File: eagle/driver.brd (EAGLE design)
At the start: 101.6 x 76.2 mm, 96 parts, among them IC1 XMEGA128A1, IC10 ST95P08M, IC11 ST95P08M, IC12 ST95P08M, IC13 ST95P08M, IC14 ST95P08M, IC15 ST95P08M, IC16 74AHC1G02DBV, IC17 74AHC1G02DBV, IC18 74AHC1G125DBV, IC19 74AHC1G125DBV, IC2 74AC16244, IC20 ST95P08M, IC21 ST95P08M, IC22 ST95P08M, IC23 ST95P08M, IC24 ST95P08M, IC25 ST95P08M, IC3 74AC16244, IC4 74AC16244, IC5 74AC16244, IC6 74AC16374, IC7 74AC16374, IC8 74AC16374, IC9 74AC16374, SW1 FSM2JSMA

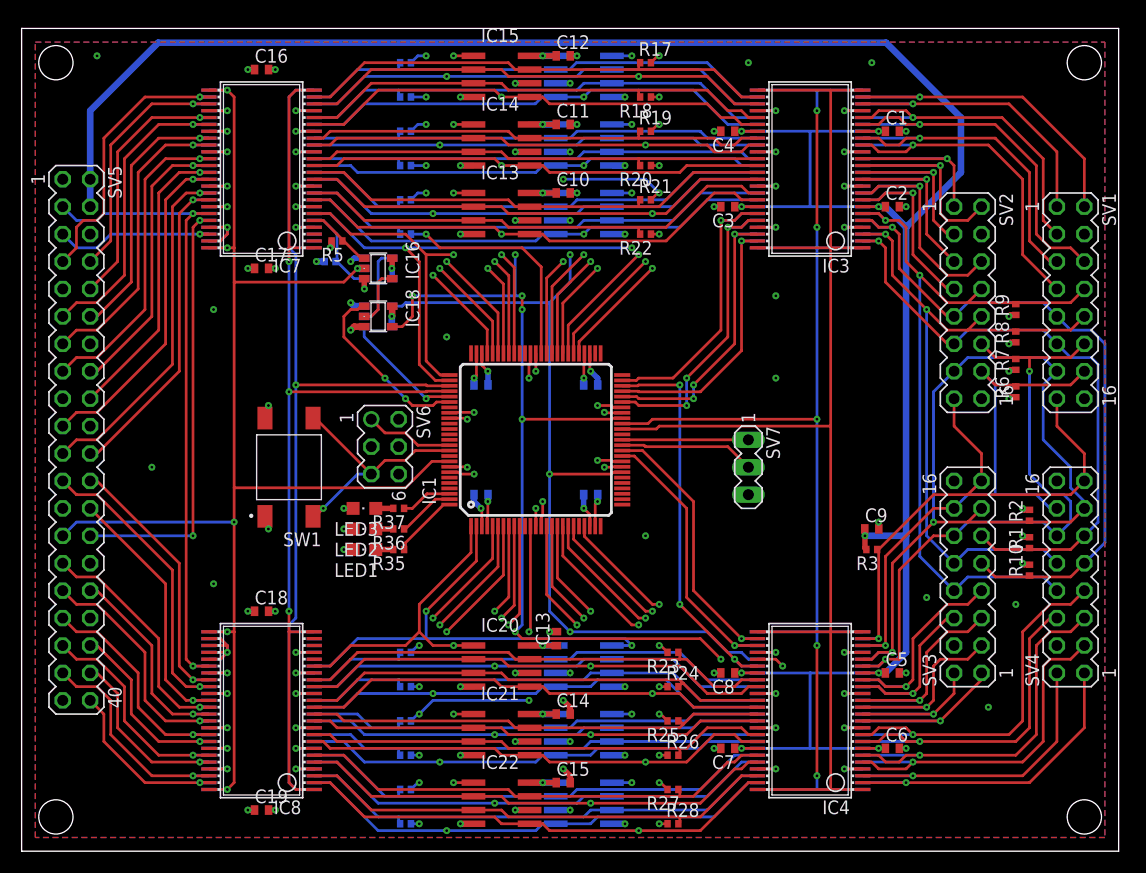
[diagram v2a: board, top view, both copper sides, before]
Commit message: adjust spacing of 16-pin headers
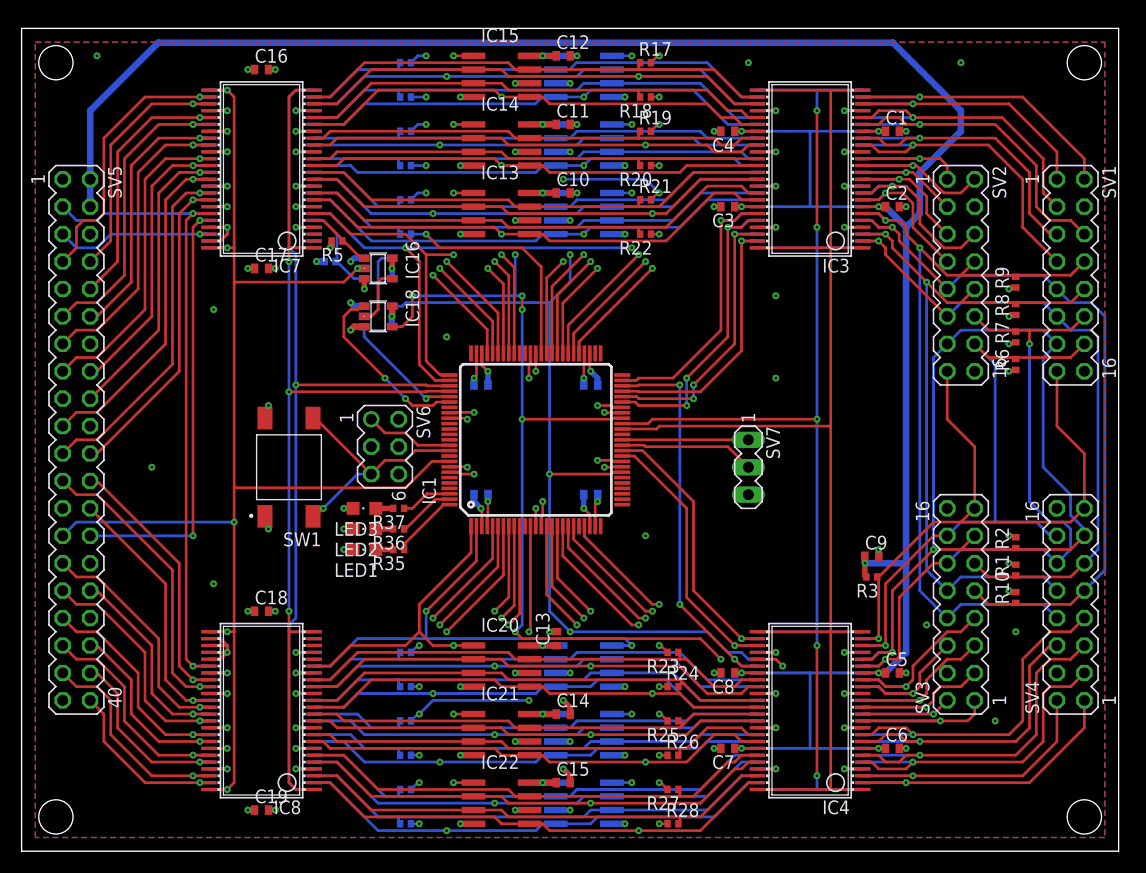
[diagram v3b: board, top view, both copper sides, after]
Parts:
- moved R1 2.84 mm to (92.1, 26.0)
- moved R10 2.84 mm to (92.1, 23.5)
- moved R2 2.84 mm to (92.1, 28.6)
- moved SV2 2.62 mm to (87.0, 53.3)
- moved SV3 2.62 mm to (87.0, 22.9)
- moved SV1 2.54 mm to (97.2, 53.3)
- moved R3 2.54 mm to (78.7, 25.4)
- moved C9 2.54 mm to (78.7, 27.3)
- moved R6 2.54 mm to (92.1, 45.1)
- moved R7 2.54 mm to (92.1, 47.6)
- moved R8 2.54 mm to (92.1, 50.2)
- moved R9 2.54 mm to (92.1, 52.7)
- moved SV4 2.54 mm to (97.2, 22.9)
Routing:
- net N$20: track 76.2 -> 84.2 mm
- net N$21: track 52.2 -> 59.8 mm
- net N$7: track 23.4 -> 16.6 mm
- net N$9: track 20.0 -> 13.2 mm
- net N$10: track 24.1 -> 17.8 mm
- net N$18: track 20.7 -> 14.4 mm
- net N$8: track 20.5 -> 14.2 mm
- net N$13: track 20.4 -> 14.6 mm
- net N$27: track 53.9 -> 57.3 mm
- net N$14: track 58.0 -> 61.2 mm
- net N$38: track 18.8 -> 15.6 mm
- net N$39: track 21.5 -> 18.3 mm
- net N$36: track 21.1 -> 18.0 mm
- net N$17: track 61.3 -> 64.5 mm
- net N$37: track 21.7 -> 18.5 mm
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
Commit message: add pull ups for register and buffer output enable lines
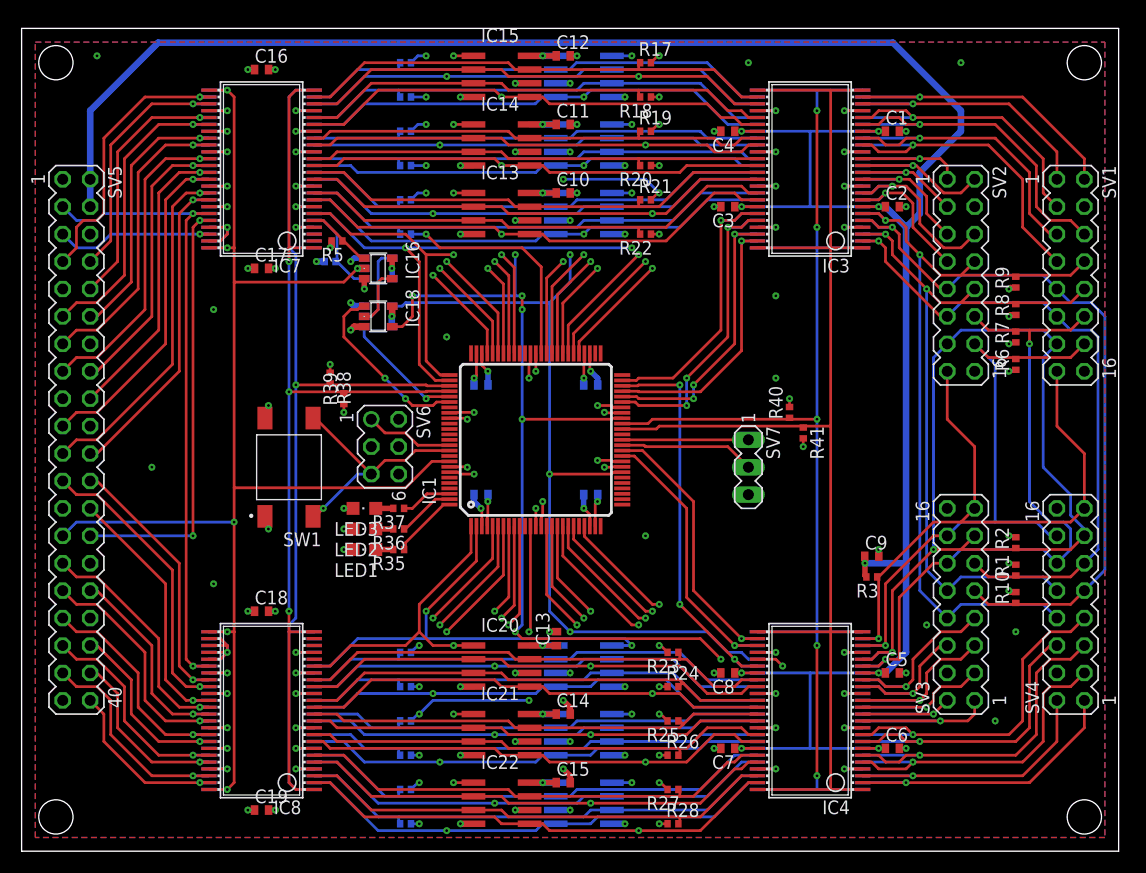
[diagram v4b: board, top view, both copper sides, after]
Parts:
- added R38, R39, R40, R41: 33k, rcl:R0402
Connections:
- net N$16: now also R41.1
- net N$19: now also R40.1
- net N$48: now also R38.2
- net N$56: now also R39.2
- net VCC: now also R38.1, R39.1, R40.2, R41.2
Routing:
- net VCC: track 83.0 -> 86.1 mm, vias 32 -> 36

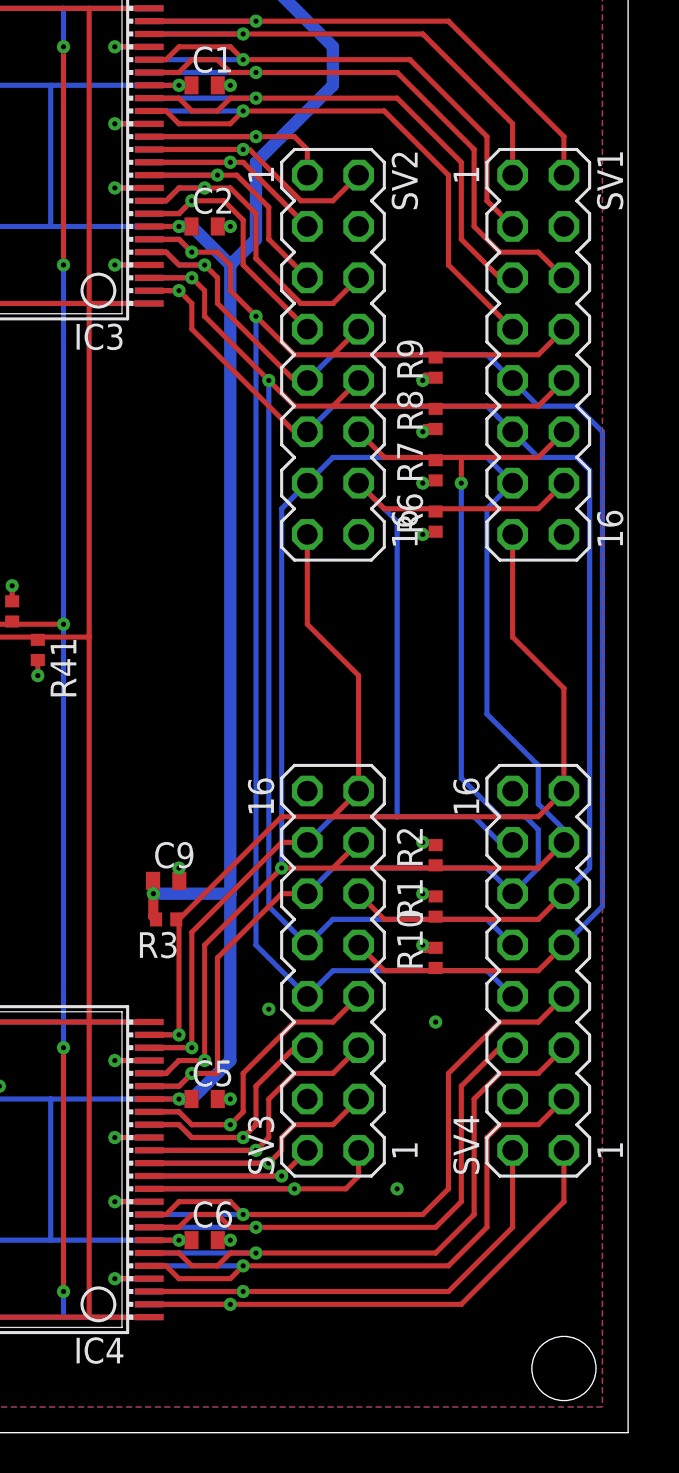
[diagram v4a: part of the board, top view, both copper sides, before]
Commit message: more spacing between panel headers
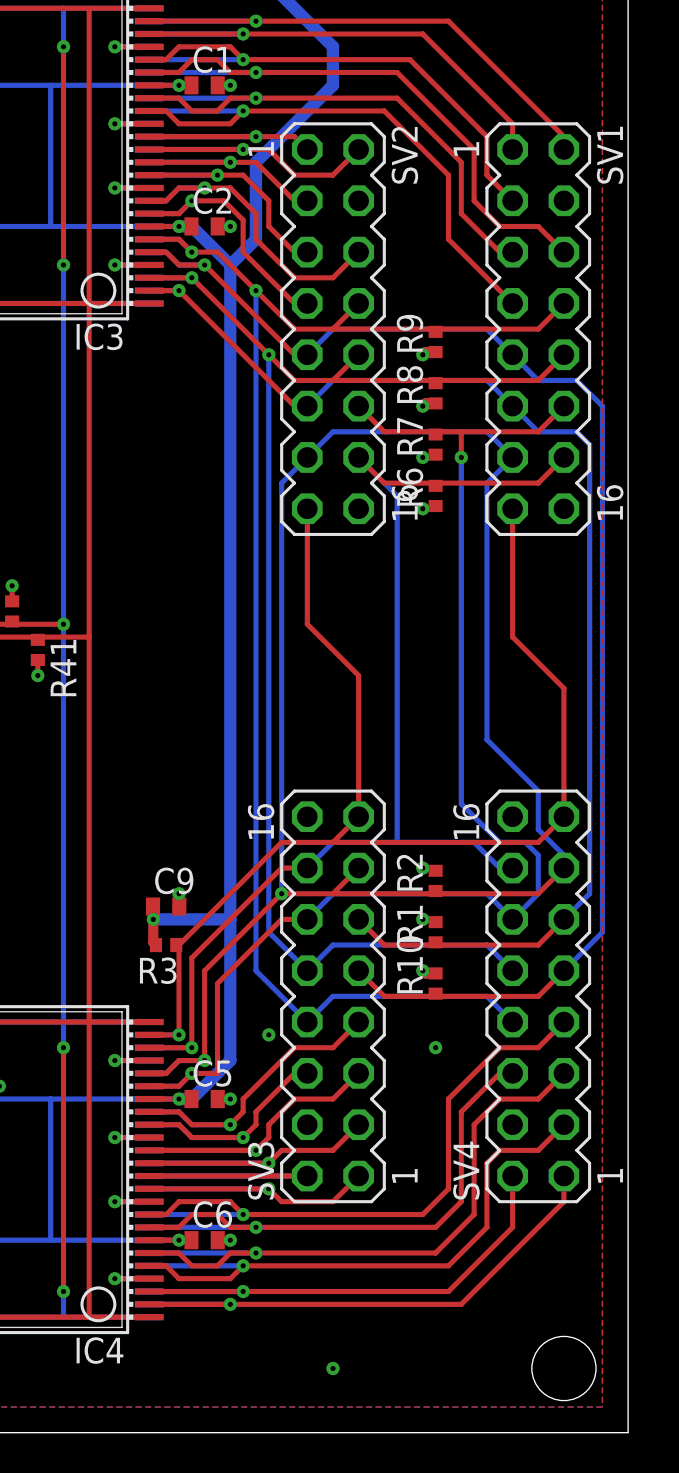
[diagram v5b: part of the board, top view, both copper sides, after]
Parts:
- moved R7 1.27 mm to (92.1, 48.9)
- moved R8 1.27 mm to (92.1, 51.4)
- moved R9 1.27 mm to (92.1, 54.0)
- moved C9 1.27 mm to (78.7, 26.0)
- moved R1 1.27 mm to (92.1, 24.8)
- moved R10 1.27 mm to (92.1, 22.2)
- moved R2 1.27 mm to (92.1, 27.3)
- moved R3 1.27 mm to (78.7, 24.1)
- moved SV3 1.27 mm to (87.0, 21.6)
- moved SV4 1.27 mm to (97.2, 21.6)
- moved R6 1.27 mm to (92.1, 46.4)
- moved SV1 1.27 mm to (97.2, 54.6)
- moved SV2 1.27 mm to (87.0, 54.6)
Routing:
- net N$20: track 84.2 -> 88.0 mm
- net N$21: track 59.8 -> 63.6 mm
- net N$32: track 19.1 -> 17.1 mm
- net N$11: track 74.4 -> 75.7 mm
- net N$17: track 64.5 -> 65.8 mm
- net N$6: track 30.2 -> 29.0 mm
- net N$5: track 29.7 -> 28.4 mm
- net N$28: track 33.5 -> 32.2 mm
- net N$25: track 33.9 -> 32.6 mm
- net N$23: track 29.2 -> 27.9 mm
- net N$2: track 27.0 -> 25.7 mm
- net N$14: track 61.6 -> 62.8 mm
- net N$13: track 14.6 -> 13.4 mm
- net N$1: track 30.1 -> 28.8 mm
- net N$4: track 28.4 -> 27.2 mm
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
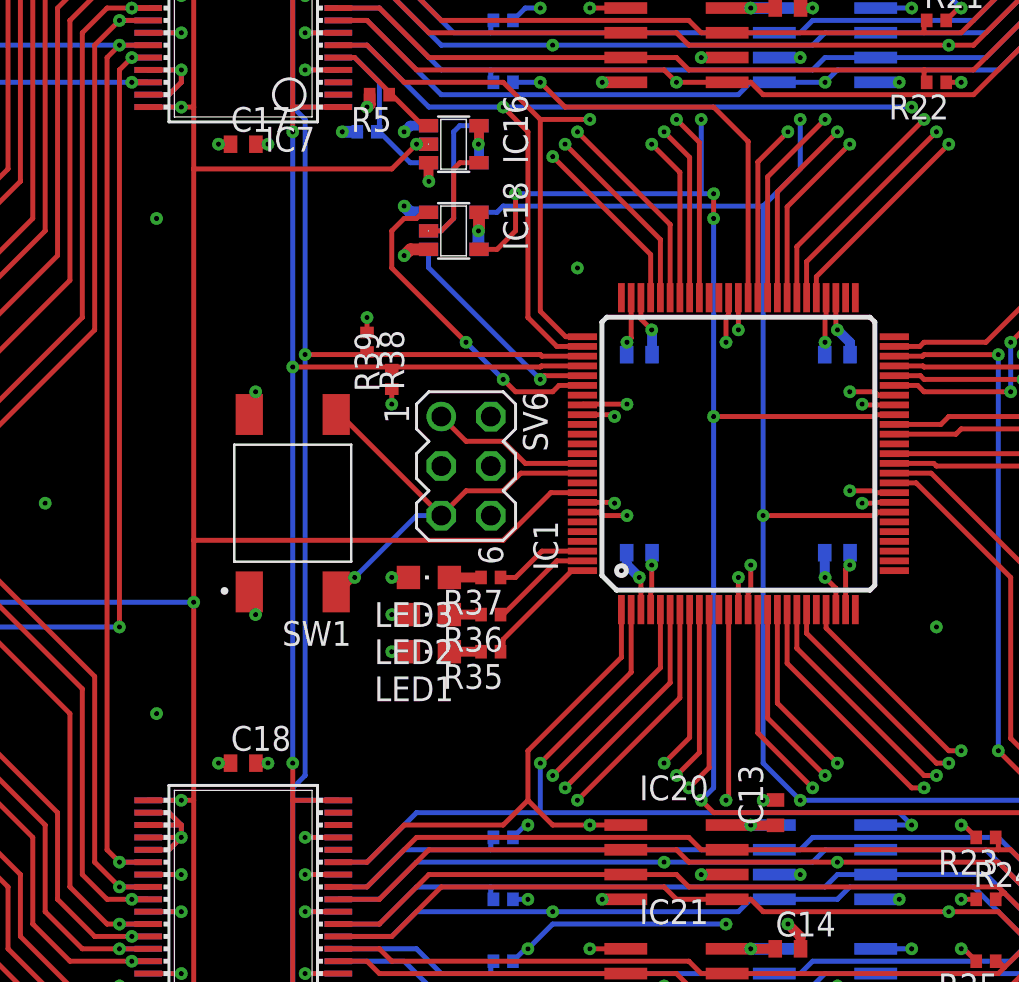
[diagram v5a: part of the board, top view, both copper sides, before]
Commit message: consolidate duplicate signals on board
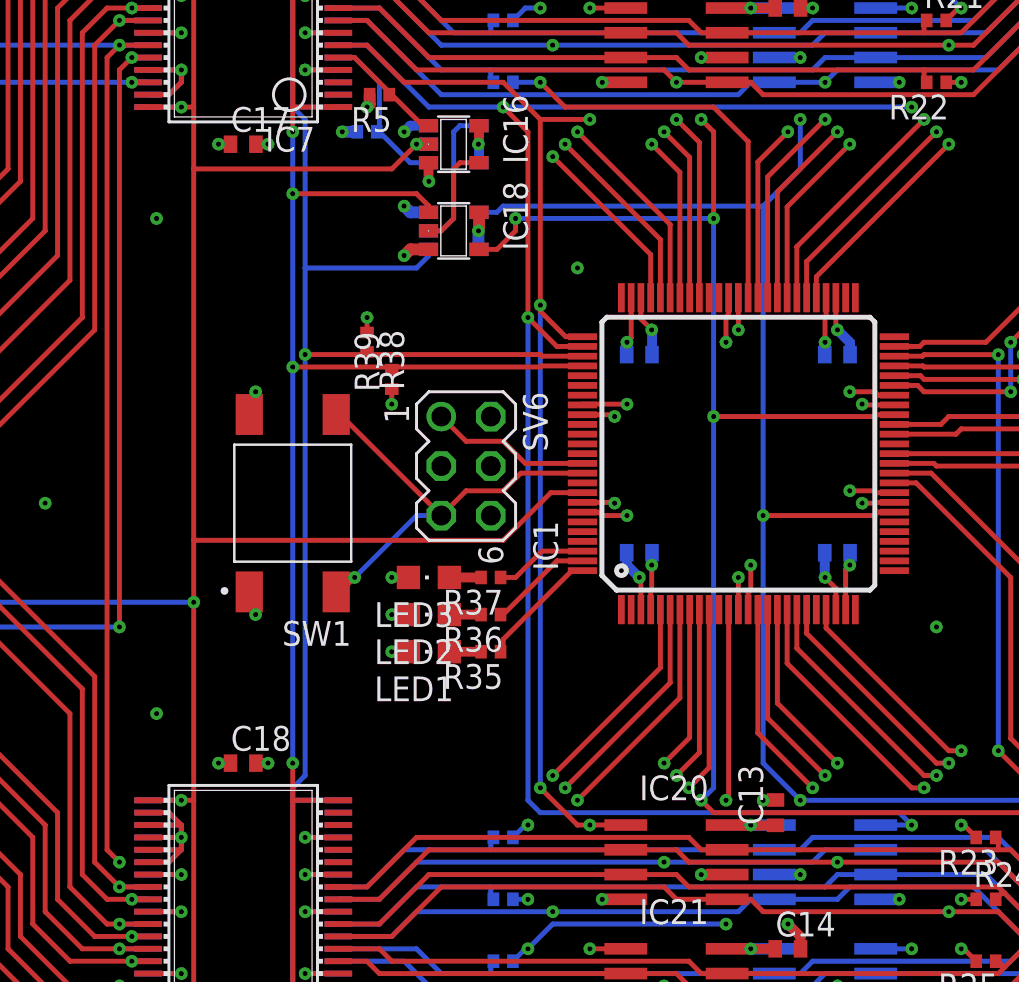
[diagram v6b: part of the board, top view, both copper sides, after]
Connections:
- net N$16 renamed OEN1
- net N$19 renamed OEN0
- removed net CLK_EN0: IC1.80, IC19.1
- removed net CLK_EN1: IC1.81, IC18.1
- removed net N$48: IC1.78, IC6.1, IC6.24, IC9.1, IC9.24, R38.2
- removed net N$56: IC1.79, IC7.1, IC7.24, IC8.1, IC8.24, R39.2
- removed net VSYNC2: IC1.1, IC20.1, IC21.1, IC22.1, IC8.19
- removed net VSYNC3: IC1.2, IC23.1, IC24.1, IC25.1, IC9.6
- new net IEN0: IC1.78, IC19.1, IC6.1, IC6.24, IC9.1, IC9.24, R38.2
- new net IEN1: IC1.79, IC18.1, IC7.1, IC7.24, IC8.1, IC8.24, R39.2
- net GND: now also IC8.30, IC9.43
- net N$94: no longer IC8.30, IC9.43
- net VSYNC0: now also IC23.1, IC24.1, IC25.1
- net VSYNC1: now also IC20.1, IC21.1, IC22.1
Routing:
- net IEN1: track 0.00 -> 96.0 mm, vias 0 -> 4
- net IEN0: track 0.00 -> 95.2 mm, vias 0 -> 1
- net N$56: track 88.4 -> 0.00 mm, vias 3 -> 0
- net N$48: track 88.3 -> 0.00 mm, vias 1 -> 0
- net VSYNC0: track 68.8 -> 132.0 mm, vias 5 -> 9
- net VSYNC3: track 61.3 -> 0.00 mm, vias 4 -> 0
- net VSYNC1: track 51.0 -> 97.3 mm, vias 4 -> 9
- net VSYNC2: track 44.7 -> 0.00 mm, vias 3 -> 0
- net CLK_EN1: track 16.7 -> 0.00 mm, vias 2 -> 0
- net CLK_EN0: track 11.3 -> 0.00 mm, vias 1 -> 0
- net GND: track 189.9 -> 194.6 mm
- net N$94: track 61.2 -> 58.2 mm
- net SCLK1: track 127.9 -> 126.9 mm, vias 14 -> 13

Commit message: fix sram chip select pins
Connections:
- removed net N$94: IC6.30, IC7.43, SV5.3
- new net VSYNC: IC1.80, IC6.30, IC7.43, SV5.3
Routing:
- net N$94: track 58.2 -> 0.00 mm, vias 2 -> 0
- net VSYNC: track 0.00 -> 52.3 mm, vias 0 -> 4
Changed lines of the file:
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@@
 <wire x1="17.3482" y1="69.85" x2="16.51" y2="69.85" width="0.254" layer="16"/>
 </signal>
-<signal name="N$94">
+<signal name="VSYNC">
 <contactref element="IC6" pad="30"/>
 <contactref element="IC7" pad="43"/>
@@
 <via x="15.875" y="59.055" extent="1-16" drill="0.254"/>
 <wire x1="17.3482" y1="59.055" x2="15.875" y2="59.055" width="0.254" layer="1"/>
-<wire x1="15.875" y1="59.055" x2="15.24" y2="58.42" width="0.254" layer="1"/>
-<wire x1="15.24" y1="17.78" x2="15.875" y2="17.145" width="0.254" layer="1"/>
-<wire x1="15.24" y1="58.42" x2="15.24" y2="17.78" width="0.254" layer="1"/>
-<via x="15.875" y="17.145" extent="1-16" drill="0.254"/>
+<contactref element="IC1" pad="80"/>
+<wire x1="39.625" y1="42.1" x2="37.655" y2="42.1" width="0.254" layer="1"/>
+<wire x1="37.655" y1="42.1" x2="37.465" y2="41.91" width="0.254" layer="1"/>
+<wire x1="36.195" y1="41.91" x2="37.465" y2="41.91" width="0.254" layer="1"/>
+<wire x1="17.3482" y1="59.055" x2="19.05" y2="59.055" width="0.254" layer="16"/>
+<wire x1="19.05" y1="59.055" x2="22.225" y2="55.88" width="0.254" layer="16"/>
+<wire x1="22.225" y1="43.815" x2="24.13" y2="41.91" width="0.254" layer="16"/>
+<via x="24.13" y="41.91" extent="1-16" drill="0.254"/>
+<wire x1="24.13" y1="41.91" x2="26.035" y2="41.91" width="0.254" layer="1"/>
+<wire x1="22.225" y1="55.88" x2="22.225" y2="43.815" width="0.254" layer="16"/>
+<via x="26.035" y="41.91" extent="1-16" drill="0.254"/>
+<via x="36.195" y="41.91" extent="1-16" drill="0.254"/>
+<wire x1="26.035" y1="41.91" x2="36.195" y2="41.91" width="0.254" layer="16"/>
 </signal>
 <signal name="N$87">
